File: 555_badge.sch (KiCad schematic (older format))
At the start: 15 parts

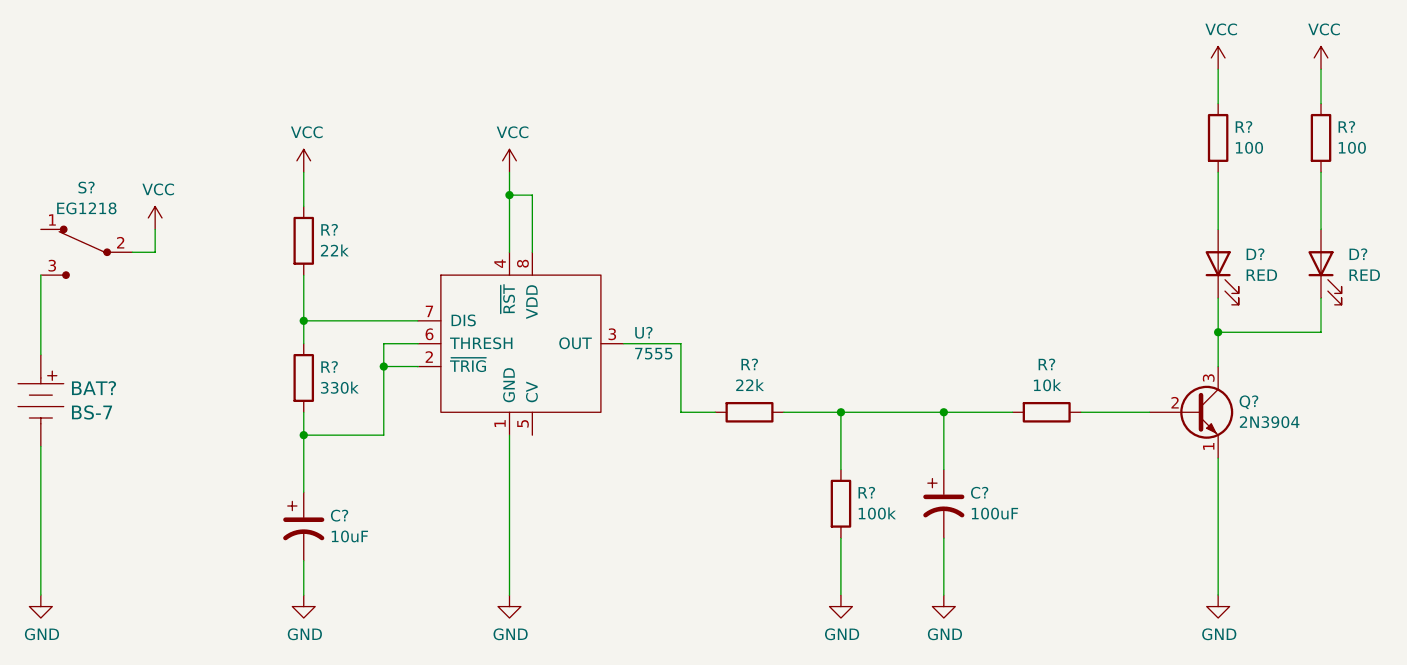
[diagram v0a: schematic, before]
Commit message: number schematic, associate schematic and footprints, and generate netlist
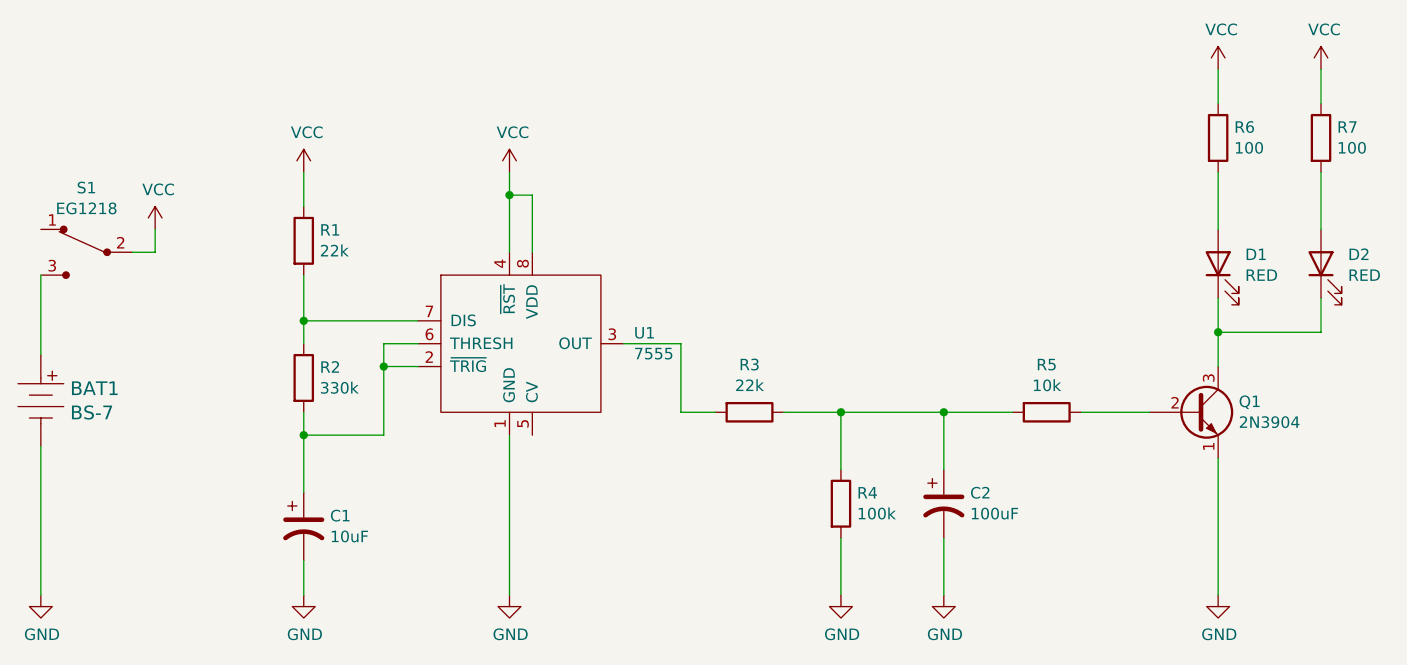
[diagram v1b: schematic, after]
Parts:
- C1: renamed from C?; footprint (none) -> Capacitor_THT:CP_Radial_D5.0mm_P2.00mm
- C2: renamed from C?; footprint (none) -> Capacitor_THT:CP_Radial_D6.3mm_P2.50mm
- D1, D2: renamed from D?; footprint (none) -> LED_THT:LED_D3.0mm
- Q1: renamed from Q?; footprint Package_TO_SOT_THT:TO-92_Inline -> digikey-footprints:TO-92-3
- R1, R2, R3, R4, R5, R6, R7: renamed from R?; footprint (none) -> Resistor_THT:R_Axial_DIN0207_L6.3mm_D2.5mm_P7.62mm_Horizontal
- U1: renamed from U?; footprint (none) -> 555_badge:ICM7555-PDIP
- gave numbers to parts that had none: 2
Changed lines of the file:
@@
 $EndDescr
 $Comp
-L 555_badge:7555 U?
+L 555_badge:7555 U1
 U 1 1 5F3C386E
 P 5950 3650
-F 0 "U?" H 6444 3696 50  0000 L CNN
+F 0 "U1" H 6444 3696 50  0000 L CNN
 F 1 "7555" H 6444 3605 50  0000 L CNN
-F 2 "" H 5950 3650 50  0001 C CNN
+F 2 "555_badge:ICM7555-PDIP" H 5950 3650 50  0001 C CNN
 F 3 "" H 5950 3650 50  0001 C CNN
 	1    5950 3650
@@
 $EndComp
 $Comp
-L Device:R R?
+L Device:R R1
 U 1 1 5F3C3D8D
 P 5000 3200
-F 0 "R?" H 5070 3246 50  0000 L CNN
+F 0 "R1" H 5070 3246 50  0000 L CNN
 F 1 "22k" H 5070 3155 50  0000 L CNN
-F 2 "" V 4930 3200 50  0001 C CNN
+F 2 "Resistor_THT:R_Axial_DIN0207_L6.3mm_D2.5mm_P7.62mm_Horizontal" V 4930 3200 50  0001 C CNN
 F 3 "~" H 5000 3200 50  0001 C CNN
 	1    5000 3200
@@
 $EndComp
 $Comp
-L Device:R R?
+L Device:R R2
 U 1 1 5F3C43AB
 P 5000 3800
-F 0 "R?" H 5070 3846 50  0000 L CNN
+F 0 "R2" H 5070 3846 50  0000 L CNN
 F 1 "330k" H 5070 3755 50  0000 L CNN
-F 2 "" V 4930 3800 50  0001 C CNN
+F 2 "Resistor_THT:R_Axial_DIN0207_L6.3mm_D2.5mm_P7.62mm_Horizontal" V 4930 3800 50  0001 C CNN
 F 3 "~" H 5000 3800 50  0001 C CNN
 	1    5000 3800
@@
 $EndComp
 $Comp
-L Device:R R?
+L Device:R R3
 U 1 1 5F3C48A5
 P 6950 3950
-F 0 "R?" V 6743 3950 50  0000 C CNN
+F 0 "R3" V 6743 3950 50  0000 C CNN
 F 1 "22k" V 6834 3950 50  0000 C CNN
-F 2 "" V 6880 3950 50  0001 C CNN
+F 2 "Resistor_THT:R_Axial_DIN0207_L6.3mm_D2.5mm_P7.62mm_Horizontal" V 6880 3950 50  0001 C CNN
 F 3 "~" H 6950 3950 50  0001 C CNN
 	1    6950 3950
@@
 $EndComp
 $Comp
-L Device:R R?
+L Device:R R4
 U 1 1 5F3C4EE9
 P 7350 4350
-F 0 "R?" H 7420 4396 50  0000 L CNN
+F 0 "R4" H 7420 4396 50  0000 L CNN
 F 1 "100k" H 7420 4305 50  0000 L CNN
-F 2 "" V 7280 4350 50  0001 C CNN
+F 2 "Resistor_THT:R_Axial_DIN0207_L6.3mm_D2.5mm_P7.62mm_Horizontal" V 7280 4350 50  0001 C CNN
 F 3 "~" H 7350 4350 50  0001 C CNN
 	1    7350 4350
@@
 $EndComp
 $Comp
-L Device:R R?
+L Device:R R5
 U 1 1 5F3C5624
 P 8250 3950
-F 0 "R?" V 8043 3950 50  0000 C CNN
+F 0 "R5" V 8043 3950 50  0000 C CNN
 F 1 "10k" V 8134 3950 50  0000 C CNN
-F 2 "" V 8180 3950 50  0001 C CNN
+F 2 "Resistor_THT:R_Axial_DIN0207_L6.3mm_D2.5mm_P7.62mm_Horizontal" V 8180 3950 50  0001 C CNN
 F 3 "~" H 8250 3950 50  0001 C CNN
 	1    8250 3950
@@
 $EndComp
 $Comp
-L Device:R R?
+L Device:R R6
 U 1 1 5F3C59C0
 P 9000 2750
-F 0 "R?" H 9070 2796 50  0000 L CNN
+F 0 "R6" H 9070 2796 50  0000 L CNN
 F 1 "100" H 9070 2705 50  0000 L CNN
-F 2 "" V 8930 2750 50  0001 C CNN
+F 2 "Resistor_THT:R_Axial_DIN0207_L6.3mm_D2.5mm_P7.62mm_Horizontal" V 8930 2750 50  0001 C CNN
 F 3 "~" H 9000 2750 50  0001 C CNN
 	1    9000 2750
@@
 $EndComp
 $Comp
-L Device:R R?
+L Device:R R7
 U 1 1 5F3C5D93
 P 9450 2750
-F 0 "R?" H 9520 2796 50  0000 L CNN
+F 0 "R7" H 9520 2796 50  0000 L CNN
 F 1 "100" H 9520 2705 50  0000 L CNN
-F 2 "" V 9380 2750 50  0001 C CNN
+F 2 "Resistor_THT:R_Axial_DIN0207_L6.3mm_D2.5mm_P7.62mm_Horizontal" V 9380 2750 50  0001 C CNN
 F 3 "~" H 9450 2750 50  0001 C CNN
 	1    9450 2750
@@
 $EndComp
 $Comp
-L Device:CP1 C?
+L Device:CP1 C1
 U 1 1 5F3C62FA
 P 5000 4450
-F 0 "C?" H 5115 4496 50  0000 L CNN
+F 0 "C1" H 5115 4496 50  0000 L CNN
 F 1 "10uF" H 5115 4405 50  0000 L CNN
-F 2 "" H 5000 4450 50  0001 C CNN
+F 2 "Capacitor_THT:CP_Radial_D5.0mm_P2.00mm" H 5000 4450 50  0001 C CNN
 F 3 "~" H 5000 4450 50  0001 C CNN
 	1    5000 4450
@@
 $EndComp
 $Comp
-L Device:CP1 C?
+L Device:CP1 C2
 U 1 1 5F3C6947
 P 7800 4350
-F 0 "C?" H 7915 4396 50  0000 L CNN
+F 0 "C2" H 7915 4396 50  0000 L CNN
 F 1 "100uF" H 7915 4305 50  0000 L CNN
-F 2 "" H 7800 4350 50  0001 C CNN
+F 2 "Capacitor_THT:CP_Radial_D6.3mm_P2.50mm" H 7800 4350 50  0001 C CNN
 F 3 "~" H 7800 4350 50  0001 C CNN
 	1    7800 4350
@@
 $EndComp
 $Comp
-L Device:LED D?
+L Device:LED D1
 U 1 1 5F3C72EF
 P 9000 3300
-F 0 "D?" V 9039 3182 50  0000 R CNN
+F 0 "D1" V 9039 3182 50  0000 R CNN
 F 1 "RED" V 8948 3182 50  0000 R CNN
-F 2 "" H 9000 3300 50  0001 C CNN
+F 2 "LED_THT:LED_D3.0mm" H 9000 3300 50  0001 C CNN
 F 3 "~" H 9000 3300 50  0001 C CNN
 	1    9000 3300
@@
 $EndComp
 $Comp
-L Device:LED D?
+L Device:LED D2
 U 1 1 5F3C7BF0
 P 9450 3300
-F 0 "D?" V 9489 3182 50  0000 R CNN
+F 0 "D2" V 9489 3182 50  0000 R CNN
 F 1 "RED" V 9398 3182 50  0000 R CNN
-F 2 "" H 9450 3300 50  0001 C CNN
+F 2 "LED_THT:LED_D3.0mm" H 9450 3300 50  0001 C CNN
 F 3 "~" H 9450 3300 50  0001 C CNN
 	1    9450 3300
@@
 $EndComp
 $Comp
-L Transistor_BJT:2N3904 Q?
+L Transistor_BJT:2N3904 Q1
 U 1 1 5F3C98A1
 P 8900 3950
-F 0 "Q?" H 9090 3996 50  0000 L CNN
+F 0 "Q1" H 9090 3996 50  0000 L CNN
 F 1 "2N3904" H 9090 3905 50  0000 L CNN
-F 2 "Package_TO_SOT_THT:TO-92_Inline" H 9100 3875 50  0001 L CIN
+F 2 "digikey-footprints:TO-92-3" H 9100 3875 50  0001 L CIN
 F 3 "https://www.fairchildsemi.com/datasheets/2N/2N3904.pdf" H 8900 3950 50  0001 L CNN
 	1    8900 3950
@@
 $EndComp
 $Comp
-L dk_Battery-Holders-Clips-Contacts:BS-7 BAT?
+L dk_Battery-Holders-Clips-Contacts:BS-7 BAT1
 U 1 1 5F3CA430
 P 3850 3900
-F 0 "BAT?" H 3978 3953 60  0000 L CNN
+F 0 "BAT1" H 3978 3953 60  0000 L CNN
 F 1 "BS-7" H 3978 3847 60  0000 L CNN
 F 2 "digikey-footprints:Battery_Holder_Coin_2032_BS-7" H 4050 4100 60  0001 L CNN
@@
 $EndComp
 $Comp
-L dk_Slide-Switches:EG1218 S?
+L dk_Slide-Switches:EG1218 S1
 U 1 1 5F3CC3A5
 P 4050 3250
-F 0 "S?" H 4050 3531 50  0000 C CNN
+F 0 "S1" H 4050 3531 50  0000 C CNN
 F 1 "EG1218" H 4050 3440 50  0000 C CNN
 F 2 "digikey-footprints:Switch_Slide_11.6x4mm_EG1218" H 4250 3450 50  0001 L CNN
@@
 $EndComp
 $Comp
-L power:GND #PWR?
+L power:GND #PWR04
 U 1 1 5F3CE200
 P 5000 4750
-F 0 "#PWR?" H 5000 4500 50  0001 C CNN
+F 0 "#PWR04" H 5000 4500 50  0001 C CNN
 F 1 "GND" H 5005 4577 50  0000 C CNN
 F 2 "" H 5000 4750 50  0001 C CNN
@@
 $EndComp
 $Comp
-L power:GND #PWR?
+L power:GND #PWR01
 U 1 1 5F3CE8ED
 P 3850 4750
-F 0 "#PWR?" H 3850 4500 50  0001 C CNN
+F 0 "#PWR01" H 3850 4500 50  0001 C CNN
 F 1 "GND" H 3855 4577 50  0000 C CNN
 F 2 "" H 3850 4750 50  0001 C CNN
@@
 $EndComp
 $Comp
-L power:GND #PWR?
+L power:GND #PWR06
 U 1 1 5F3CEC14
 P 5900 4750
-F 0 "#PWR?" H 5900 4500 50  0001 C CNN
+F 0 "#PWR06" H 5900 4500 50  0001 C CNN
 F 1 "GND" H 5905 4577 50  0000 C CNN
 F 2 "" H 5900 4750 50  0001 C CNN
@@
 $EndComp
 $Comp
-L power:GND #PWR?
+L power:GND #PWR07
 U 1 1 5F3CEE86
 P 7350 4750
-F 0 "#PWR?" H 7350 4500 50  0001 C CNN
+F 0 "#PWR07" H 7350 4500 50  0001 C CNN
 F 1 "GND" H 7355 4577 50  0000 C CNN
 F 2 "" H 7350 4750 50  0001 C CNN
@@
 $EndComp
 $Comp
-L power:GND #PWR?
+L power:GND #PWR08
 U 1 1 5F3CF2BE
 P 7800 4750
-F 0 "#PWR?" H 7800 4500 50  0001 C CNN
+F 0 "#PWR08" H 7800 4500 50  0001 C CNN
 F 1 "GND" H 7805 4577 50  0000 C CNN
 F 2 "" H 7800 4750 50  0001 C CNN
@@
 $EndComp
 $Comp
-L power:GND #PWR?
+L power:GND #PWR010
 U 1 1 5F3CF5EA
 P 9000 4750
-F 0 "#PWR?" H 9000 4500 50  0001 C CNN
+F 0 "#PWR010" H 9000 4500 50  0001 C CNN
 F 1 "GND" H 9005 4577 50  0000 C CNN
 F 2 "" H 9000 4750 50  0001 C CNN
@@
 $EndComp
 $Comp
-L power:VCC #PWR?
+L power:VCC #PWR02
 U 1 1 5F3CFC6E
 P 4350 3150
-F 0 "#PWR?" H 4350 3000 50  0001 C CNN
+F 0 "#PWR02" H 4350 3000 50  0001 C CNN
 F 1 "VCC" H 4365 3323 50  0000 C CNN
 F 2 "" H 4350 3150 50  0001 C CNN
@@
 $EndComp
 $Comp
-L power:VCC #PWR?
+L power:VCC #PWR03
 U 1 1 5F3D04FA
 P 5000 2900
-F 0 "#PWR?" H 5000 2750 50  0001 C CNN
+F 0 "#PWR03" H 5000 2750 50  0001 C CNN
 F 1 "VCC" H 5015 3073 50  0000 C CNN
 F 2 "" H 5000 2900 50  0001 C CNN
@@
 $EndComp
 $Comp
-L power:VCC #PWR?
+L power:VCC #PWR05
 U 1 1 5F3D0991
 P 5900 2900
-F 0 "#PWR?" H 5900 2750 50  0001 C CNN
+F 0 "#PWR05" H 5900 2750 50  0001 C CNN
 F 1 "VCC" H 5915 3073 50  0000 C CNN
 F 2 "" H 5900 2900 50  0001 C CNN
@@
 $EndComp
 $Comp
-L power:VCC #PWR?
+L power:VCC #PWR09
 U 1 1 5F3D1715
 P 9000 2450
-F 0 "#PWR?" H 9000 2300 50  0001 C CNN
+F 0 "#PWR09" H 9000 2300 50  0001 C CNN
 F 1 "VCC" H 9015 2623 50  0000 C CNN
 F 2 "" H 9000 2450 50  0001 C CNN
@@
 $EndComp
 $Comp
-L power:VCC #PWR?
+L power:VCC #PWR011
 U 1 1 5F3D1B84
 P 9450 2450
-F 0 "#PWR?" H 9450 2300 50  0001 C CNN
+F 0 "#PWR011" H 9450 2300 50  0001 C CNN
 F 1 "VCC" H 9465 2623 50  0000 C CNN
 F 2 "" H 9450 2450 50  0001 C CNN
